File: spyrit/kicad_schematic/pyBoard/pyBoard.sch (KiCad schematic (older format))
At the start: 83 parts, among them J1 USB_OTG, P1 CONN_01X02, SW1-RST1 SPST, SW2-USR1 SPST, U1 MCP1754ST-1802E/MB, U2 SPIRIT1, U3 STM32F405RGTx, U4 TPS22933, Y1 Crystal, Y2 8MHz

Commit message: [Derek] created custom package UQFP and subsequently finished the netlist
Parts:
- C1, C10, C11, C12, C13, C14, C15, C16, C17, C18, C19, C2, C20, C21, C22, C23, C24, C25, C26, C27, C28, C29, C3, C30, C4, C5, C6, C7, C8, C9: footprint (none) -> Capacitors_SMD:C_0805_HandSoldering
- D1, D1p1, D2, D2p1, D3, D3p1, D4, D4p1: footprint (none) -> LEDs:LED_0805
- D5: footprint (none) -> Diodes_SMD:DD-PAK_TO263_SingleDiode
- J1: footprint (none) -> Connect:USB_Micro-B
- L1, L10, L11, L2, L3, L4, L5, L6, L7, L8, L9: footprint (none) -> Choke_SMD:Choke_SMD_1206_Handsoldering
- P1: footprint (none) -> Socket_Strips:Socket_Strip_Straight_1x02
- R1, R10, R11, R12, R13, R14, R15, R16, R17, R18, R19, R2, R20, R21, R22, R3, R4, R5, R6, R7, R8, R9, R9]1: footprint (none) -> Resistors_SMD:R_0805_HandSoldering
- SW1-RST1, SW2-USR1: footprint (none) -> Buttons_Switches_SMD:SW_SPST_B3S-1100
- U1: footprint (none) -> TO_SOT_Packages_SMD:SOT89-3_Housing_Handsoldering
- U2: footprint (none) -> Housings_DFN_QFN:QFN-20-1EP_4x4mm_Pitch0.5mm
- U4: footprint (none) -> external_Housings_DFN_QFN:UQFN_1.5mm_x_1.5mm
- Y1, Y2: footprint (none) -> Oscillators:SI570_SI571_HandSoldering

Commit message: [Derek] inital commit for PCB layout, FIRECODE schematic v2.0 up
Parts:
- U3: footprint LQFP64 -> Housings_QFP:LQFP-64_10x10mm_Pitch0.5mm
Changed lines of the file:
@@
 F 0 "U3" H 7600 6975 50  0000 C CNN
 F 1 "STM32F405RGTx" H 16000 6975 50  0000 R BNN
-F 2 "LQFP64" H 16000 6925 50  0000 R TNN
+F 2 "Housings_QFP:LQFP-64_10x10mm_Pitch0.5mm" H 16000 6925 50  0000 R TNN
 F 3 "" H 11800 5050 50  0000 C CNN
 	1    11800 5050

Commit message: [Derek] wiring intial commit
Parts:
- removed R16, R9]1: 4k7, Resistors_SMD:R_0805_HandSoldering, symbol R
- removed R5: R, Resistors_SMD:R_0805_HandSoldering, symbol R
- removed SW2-USR1: SPST, Buttons_Switches_SMD:SW_SPST_B3S-1100, symbol SPST
- D5: footprint Diodes_SMD:DD-PAK_TO263_SingleDiode -> Diodes_SMD:SMB_Handsoldering
- P1: footprint Socket_Strips:Socket_Strip_Straight_1x02 -> Connect:PINHEAD1-3; symbol CONN_01X02 -> CONN_01X03
- Y1, Y2: footprint Oscillators:SI570_SI571_HandSoldering -> Crystals:Crystal_SMD_5032_2Pads
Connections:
- net RST#: now also P1.3 (P3); no longer C2.1, R1.2, SW1-RST1.1, U3.7 (NRST)
- net at U4.1 (VBAT): now also P1.1 (P1); no longer P1.2 (P2)
- net at U4.3 (DC_IN): now also P1.2 (P2); no longer P1.1 (P1)
- net PB6-SCL-X9: no longer names the net of U3.58 (CAN2_TX/I2C1_SCL/TIM4_CH1/USART1_TX/PB6)
- net PB7-SDA-X10: no longer names the net of U3.59 (I2C1_SDA/TIM4_CH2/USART1_RX/PB7)
- new net: C2.1, R1.2, SW1-RST1.1, U3.7 (NRST)
- no-connect marks 25 -> 27
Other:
- note added: "Ports related to\nunused header pins:\nPA0-PA7, PB3, PB6-PB7"
- note removed: "Ports related to\nunused header pins:\nPA0-PA7, PB3"
- moved on the sheet: C1, C11, C14, C15, C16, C17, C18, C19, C20, C21, C22, C23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

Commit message: [Derek] updating to FIRECODE schematic v3
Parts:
- SW1-RST1: footprint Buttons_Switches_SMD:SW_SPST_B3S-1100 -> Buttons_Switches_SMD:SW_SPST_B3U-3000P-B
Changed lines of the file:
@@
 F 0 "SW1-RST1" H 2300 4250 50  0000 C CNN
 F 1 "SPST" H 2300 4050 50  0000 C CNN
-F 2 "Buttons_Switches_SMD:SW_SPST_B3S-1100" H 2300 4150 50  0001 C CNN
+F 2 "Buttons_Switches_SMD:SW_SPST_B3U-3000P-B" H 2300 4150 50  0001 C CNN
 F 3 "" H 2300 4150 50  0000 C CNN
 	1    2300 4150

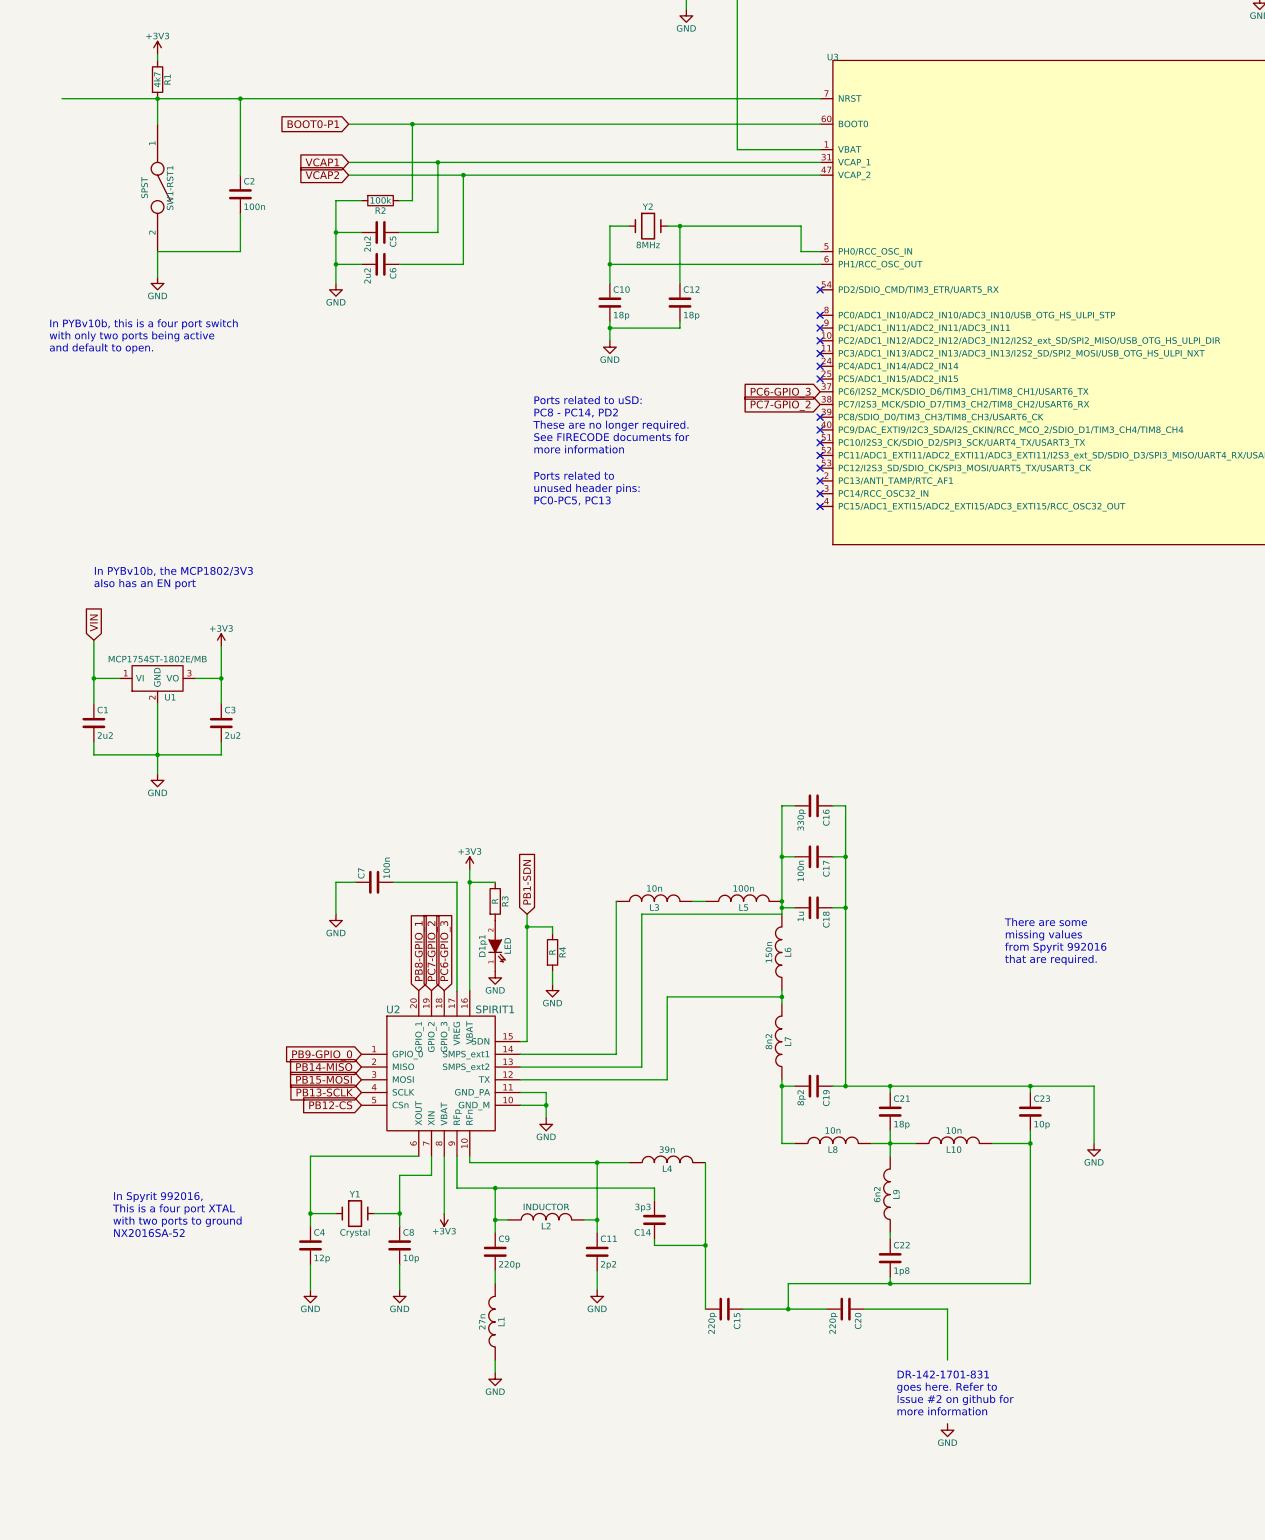
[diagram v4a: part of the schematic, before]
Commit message: [Derek] implementing 5/9 of pcb review improvements
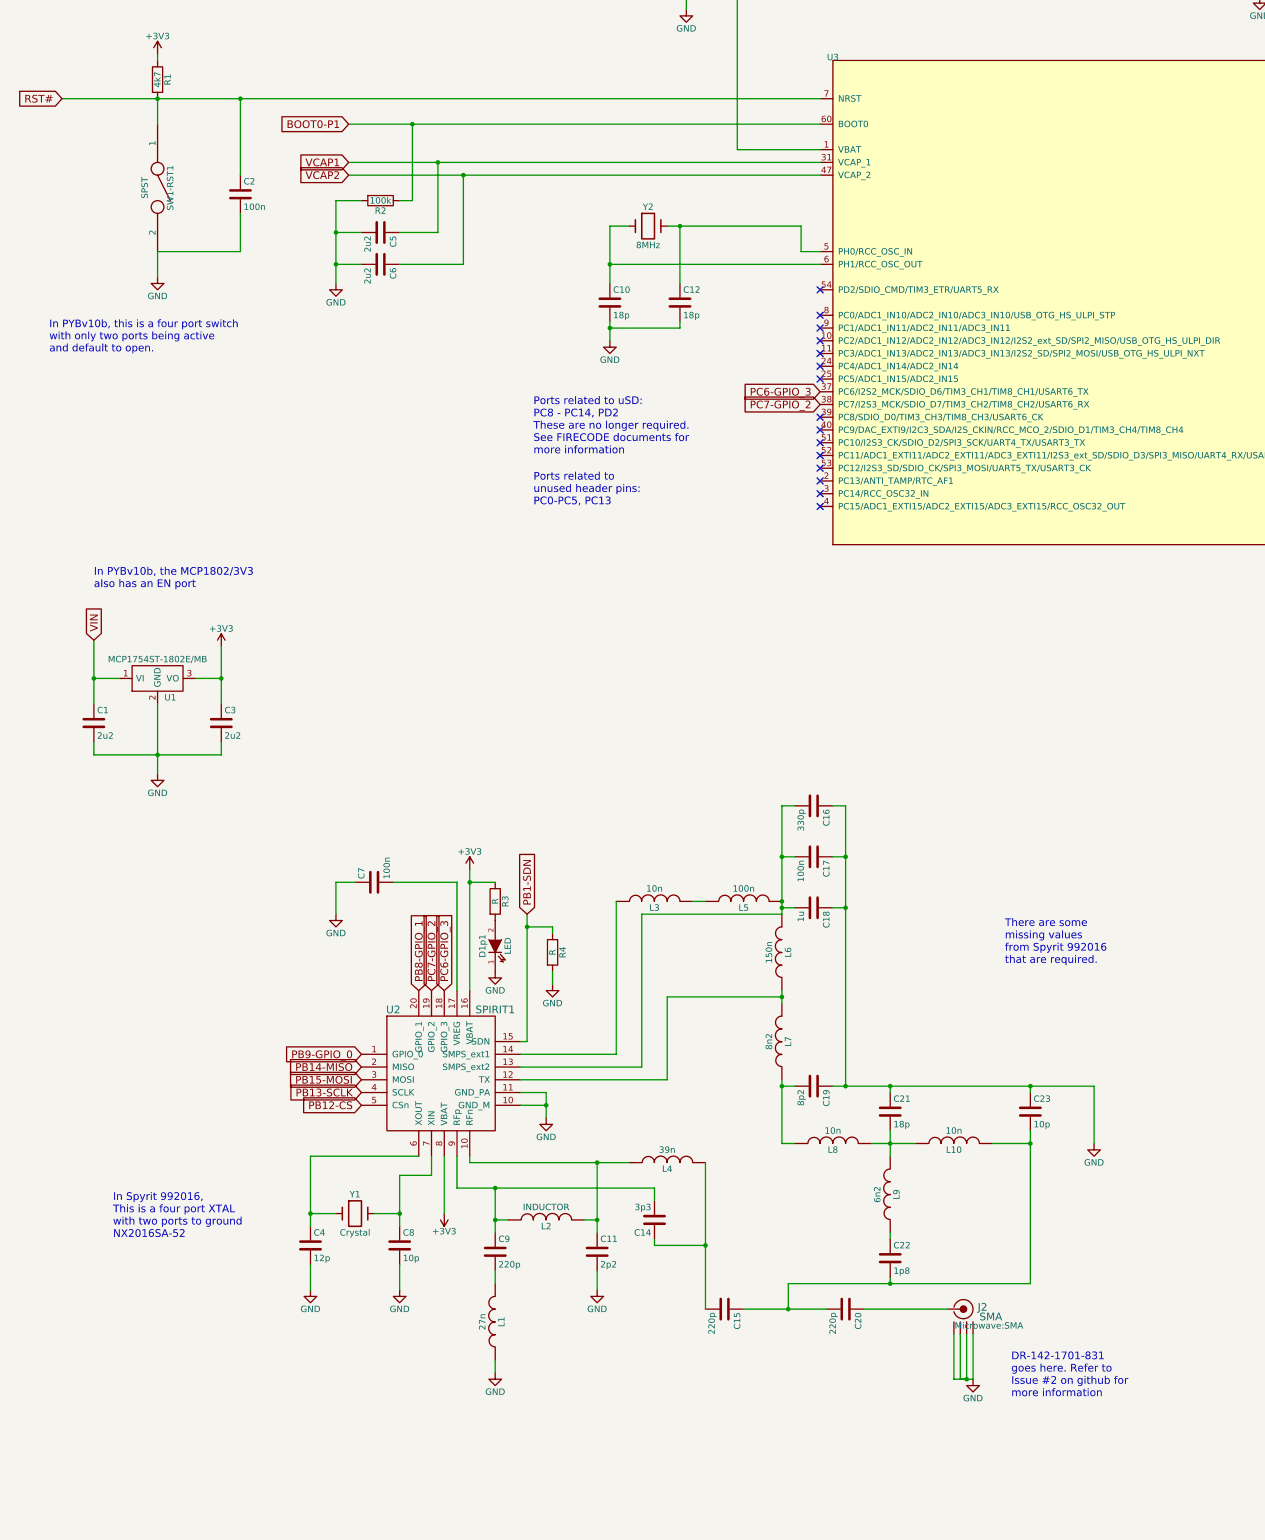
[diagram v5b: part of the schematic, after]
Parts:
- added J2: SMA, Microwave:SMA, symbol SMA
- C1, C10, C11, C12, C13, C14, C15, C16, C17, C18, C19, C2, C20, C21, C22, C23, C24, C25, C26, C27, C28, C29, C3, C30, C4, C5, C6, C7, C8, C9: footprint Capacitors_SMD:C_0805_HandSoldering -> Capacitors_SMD:C_0603_HandSoldering
- D1, D1p1, D2, D2p1, D3, D3p1, D4, D4p1: footprint LEDs:LED_0805 -> LEDs:LED_0603
- R1, R10, R11, R12, R13, R14, R15, R17, R18, R19, R2, R20, R21, R22, R3, R4, R6, R7, R8, R9: footprint Resistors_SMD:R_0805_HandSoldering -> Resistors_SMD:R_0603_HandSoldering
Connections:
- net GND: now also J2.2 (GND1), J2.3 (GND2), J2.4 (GND3), J2.5 (GND4)
- net RST#: now also C2.1, R1.2, SW1-RST1.1, U3.7 (NRST)
- net at C20.1: now also J2.1 (RF)
